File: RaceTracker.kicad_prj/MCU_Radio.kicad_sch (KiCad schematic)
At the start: 46 parts, among them J12 SWD-Programmierheader, Q1 2N7002, Q5 BSS138PS, U1 D21G18, U2 NINA-W102, Y1 32768Hz

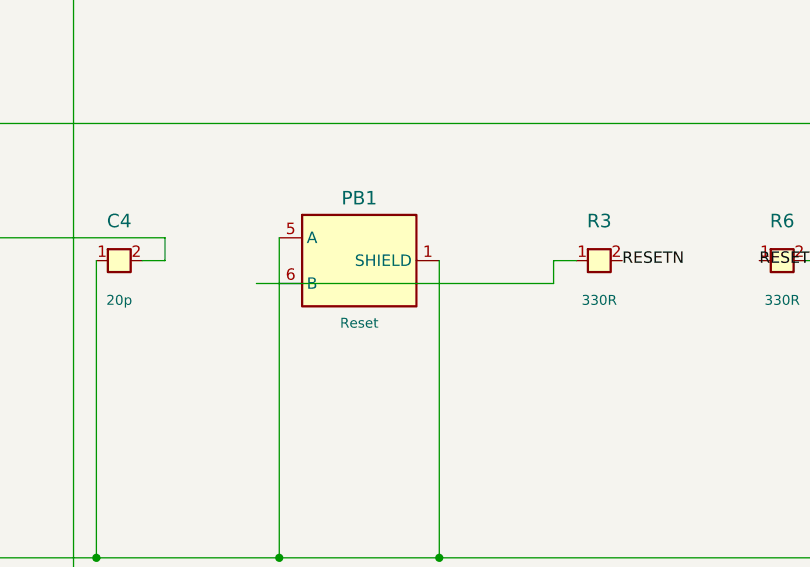
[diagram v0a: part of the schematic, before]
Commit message: ERC auf 0/0: J1.CC2/R38, J7-Draht und PB1/R3 verbunden, VBUS-Cap ergänzt
Echte KiCad-ERC (kicad-cli sch erc) fand 7 Verstöße, alle auf dasselbe
Muster zurückgeführt: ein Bauteil-Pin lag exakt auf einem Draht, aber
ohne Endpunkt-Treffer oder Junction erkannt daher KiCad ihn nicht als
verbunden. Behoben durch Draht-Trimming auf die exakte Pin-Position,
verifiziert per kicad-cli-Netzlisten-Diff (nur die betroffenen Pins
ändern sich, sonst nichts an den 128 Bauteilen):

- Power.kicad_sch: J1.CC2 <-> R38 (5,1k Pulldown) verbunden, gleicher
  Fehlertyp wie der CC1/GND-Kurzschluss aus dem letzten Commit, nur
  diesmal eine offene statt einer kurzgeschlossenen Verbindung
- Power.kicad_sch: J7.BATT+ Draht-Überstand über den Steckerkörper
  hinaus entfernt
- MCU_Radio.kicad_sch: PB1 (Reset-Taster) Pin 6 <-> R3 verbunden
- Power.kicad_sch: C34 (1uF) als VBUS-Entkopplung an J1 ergänzt, war
  direkt am USB-C-Stecker komplett unbestückt

Per Datenblatt (TI BQ24195L, u-blox ZED-F9P) als Fehlalarme der
kicad-happy-Analyse verifiziert, keine Änderung nötig: I2C_SCL/SDA
Spannungsdomäne (SCL/SDA sind Open-Drain), STAT/CE fehlender Pull-up
(STAT hat LED+R23, CE hat bewusst R25 als Pull-down), RTK_STAT/GEO_STAT
(Push-Pull-Ausgänge), CHG_VBUS ohne DC-Pfad (Analyzer modelliert keine
Transistor-Leitpfade, Q2 ist ein Standard-P-FET-Passschalter).

Co-Authored-By: Claude Sonnet 5 <noreply@anthropic.com>
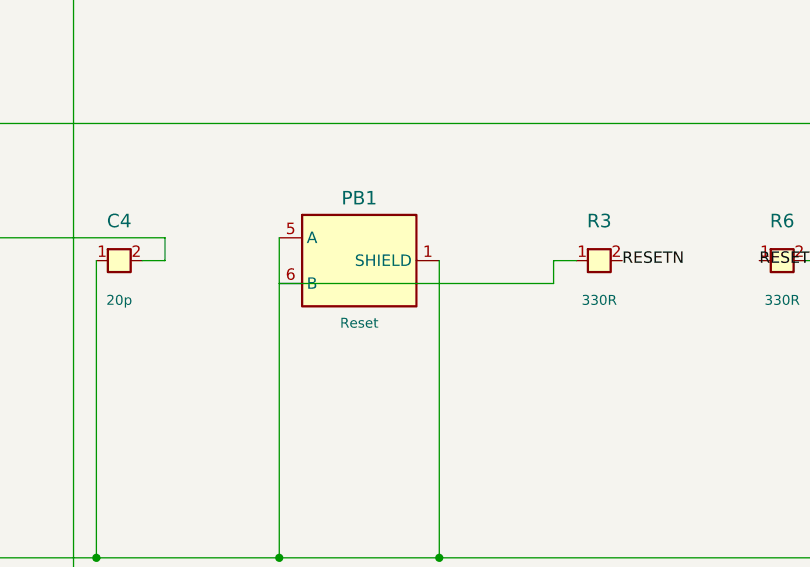
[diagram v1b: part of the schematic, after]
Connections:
- net at R3.1: now also PB1.6 (B)
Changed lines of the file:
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@@
 	(wire
 		(pts
-			(xy 78.74 156.21) (xy 111.76 156.21)
+			(xy 81.28 156.21) (xy 111.76 156.21)
 		)
 		(stroke

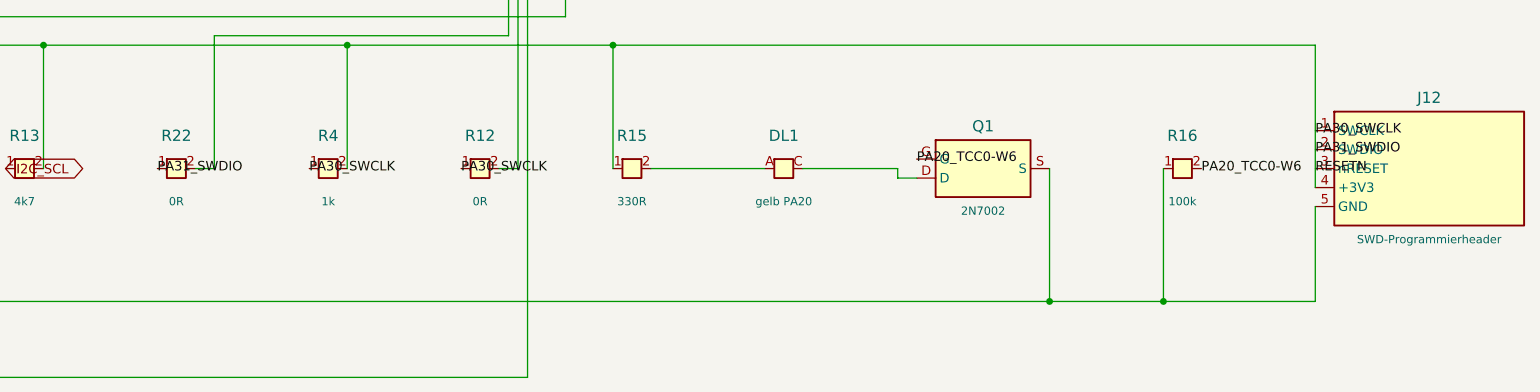
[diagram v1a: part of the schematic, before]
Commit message: Referenzabgleich gegen MKR-WiFi-1010-Eagle-Schaltplan: 2 Abweichungen behoben
Systematischer Netz-für-Netz-Vergleich zwischen der originalen Eagle-
Referenz (MKRWiFi1010V2.0.sch) und der aktuellen KiCad-Netzliste ergab
78 von 85 Netzen exakt identisch. Die restlichen 7 waren bis auf zwei
reine Pin-Namens-/Nummerierungsunterschiede zwischen Eagle- und
KiCad-Symbolen (Q5 Multi-Gate-Split, PB1-Kontaktnummerierung, J7/Q2
Pin-Namen) — keine echten Fehler.

Zwei echte Abweichungen behoben:

- MCU_Radio.kicad_sch: Serienwiderstand R2 (39R) am Reset-Pin des
  SWD-Headers ergänzt. War beim Umbau von MKR-Debug-Header (J2,
  entfallen) auf den neuen SWD-Header (J12) verlorengegangen — SWCLK
  (R4/R12) und SWDIO (R22) hatten ihre Schutzwiderstände behalten,
  nur nRESET nicht. J12.3 hängt jetzt über R2 am RESETN-Netz statt
  direkt.
- Power.kicad_sch: Label "VIN" am Netz R19.2/Q2.Gate/Q2.Anode wieder
  ergänzt (elektrisch war die Verbindung bereits korrekt, nur ohne
  Beschriftung als automatisch benanntes Netz sichtbar).

Beide Änderungen per kicad-cli-Netzlisten-Diff verifiziert (nur die
vier betroffenen Pins ändern sich), ERC weiterhin 0 Fehler/0 Warnungen.

Co-Authored-By: Claude Sonnet 5 <noreply@anthropic.com>
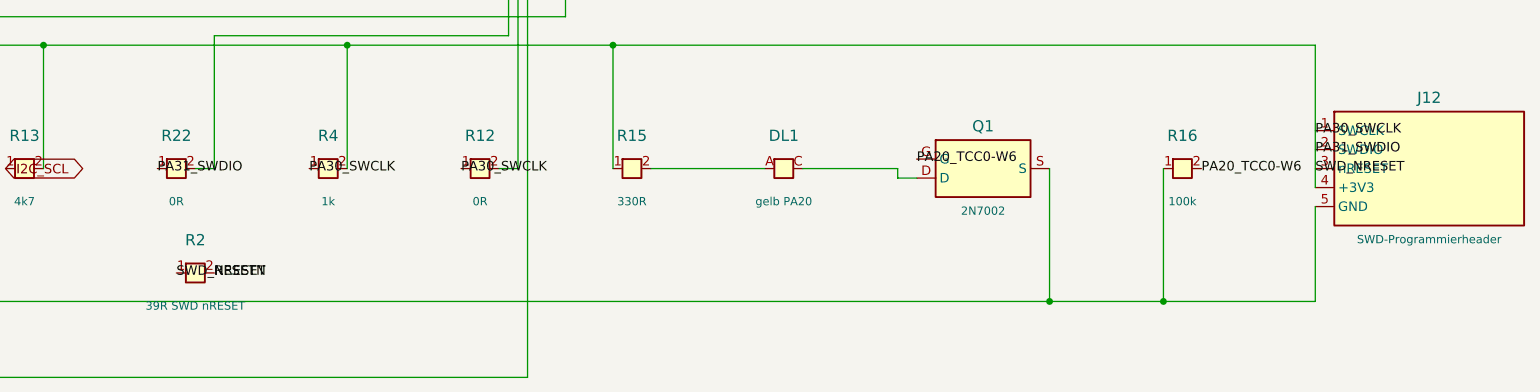
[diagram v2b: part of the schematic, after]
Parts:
- added R2: 39R SWD nRESET, symbol RaceTracker:R_GENERIC
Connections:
- net +3V3: now also R2.1; no longer C2.1, R3.2, R5.1, R6.1, U1.40 (RESETN)
- new net RESETN: C2.1, R2.2, R3.2, R5.1, R6.1, U1.40 (RESETN)
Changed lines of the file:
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@@
 		)
 	)
-	(label "RESETN"
+	(label "SWD_NRESET"
 		(at 400.05 217.17 0)
 		(effects
@@
 		)
 	)
+	(symbol
+		(lib_id "RaceTracker:R_GENERIC")
+		(at 250.19 231.14 0)
+		(unit 1)
+		(body_style 1)
+		(exclude_from_sim no)
+		(in_bom yes)
+		(on_board yes)
+		(in_pos_files yes)
+		(dnp no)
+		(property "Reference" "R2"
+			(at 250.19 226.74 0)
+			(show_name no)
+			(do_not_autoplace no)
+			(effects
+				(font
+					(size 1.5 1.5)
+				)
+			)
+		)
+		(property "Value" "39R SWD nRESET"
+			(at 250.19 235.54 0)
+			(show_name no)
+			(do_not_autoplace no)
+			(effects
+				(font
+					(size 1.1 1.1)
+				)
+			)
+		)
+		(property "Footprint" ""
+			(at 250.19 231.14 0)
+			(hide yes)
+			(show_name no)
+			(do_not_autoplace no)
+			(effects
+				(font
+					(size 1.27 1.27)
+				)
+			)
+		)
+		(property "Datasheet" ""
+			(at 250.19 231.14 0)
+			(hide yes)
+			(show_name no)
+			(do_not_autoplace no)
+			(effects
+				(font
+					(size 1.27 1.27)
+				)
+			)
+		)
+		(property "Description" ""
+			(at 250.19 231.14 0)
+			(show_name no)
+			(do_not_autoplace no)
+			(effects
+				(font
+					(size 1.27 1.27)
+				)
+			)
+		)
+		(pin "1"
+		)
+		(pin "2"
+		)
+		(instances
+			(project "RaceTracker"
+				(path "/91b37a92-c006-41eb-be41-a2390c5c45b2/2eab94b4-4968-4af9-95bb-7d350df3d3fd"
+					(reference "R2")
+					(unit 1)
+				)
+			)
+		)
+	)
+	(label "SWD_NRESET"
+		(at 247.65 231.14 0)
+		(effects
+			(font
+				(size 1.27 1.27)
+			)
+			(justify left)
+		)
+	)
+	(label "RESETN"
+		(at 252.73 231.14 0)
+		(effects
+			(font
+				(size 1.27 1.27)
+			)
+			(justify left)
+		)
+	)

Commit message: Footprints für Power+MCU_Radio: aus MKR1010-Eagle-Referenz importiert
Nutzt kicad-cli pcb import, um die reale MKR-WiFi-1010-Platine
(user-bereitgestellt, MKRWiFi1010V2.0.brd) nach KiCad zu konvertieren
und daraus bewährte, aus einem tatsächlich gefertigten Board stammende
Footprint-Geometrien zu extrahieren statt sie zu schätzen:

- 15 spezielle Footprints neu in RaceTracker.pretty/ (SOT-143B für D1,
  SOD-323FL für D2/D3, SOT-523 für Q1/Q3, SON-8 für Q2, SOT-363 für Q5,
  JST-PH für J7, PTS820-Taster, 0603-LED, RGB-5050-LED, SRP4020-Spule,
  32.768kHz-Quarz ABS07)
- 3 bestehende Custom-Footprints (QFN24, QFN48/SAMD21, NINA-W1X) durch
  die vollständigeren Eagle-Varianten ersetzt (identische Pad-Namen
  verifiziert, jetzt mit Silkscreen-Outline und Lötstoppmasken-Angaben)
- Alle Standard-Passiva (R/C 0402/0603/0805, Fuse, Ferritperle) auf
  KiCads Standardbibliothek gemappt
- J12 (SWD-Header) auf Standard-2,54mm-5-Pin-Stiftleiste gemappt

87 von 90 Bauteilen auf Power+MCU_Radio haben jetzt ein Footprint
(Rest: GPS- und Sensors_Storage-Blatt folgen). ERC weiterhin 0/0,
inklusive der Footprint-Bibliotheksprüfung (jeder Footprint-Name
gegen die echte Bibliothek verifiziert).

Co-Authored-By: Claude Sonnet 5 <noreply@anthropic.com>
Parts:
- C17, C18, C2, C21, C23, C24, C25, C26, C3, C4, C5, C6, C7: footprint (none) -> Capacitor_SMD:C_0402_1005Metric
- C27: footprint (none) -> Capacitor_SMD:C_0603_1608Metric
- DL1: footprint (none) -> RaceTracker:LED_0603_AK
- DL4: footprint (none) -> RaceTracker:RGBLED_5050
- J12: footprint (none) -> Connector_PinHeader_2.54mm:PinHeader_1x05_P2.54mm_Vertical
- L3: footprint (none) -> Inductor_SMD:L_0603_1608Metric
- PB1: footprint (none) -> RaceTracker:PTS820_NO_HOLES
- Q1: footprint (none) -> RaceTracker:SOTFL50P160X78-3
- Q5: footprint (none) -> RaceTracker:SOT363
- R10, R11, R12, R13, R14, R15, R16, R17, R18, R2, R20, R21, R22, R3, R34, R35, R36, R4, R5, R6, R7, R8, R9: footprint (none) -> Resistor_SMD:R_0402_1005Metric
- U1: footprint (none) -> RaceTracker:QFN48_SAMD21G18A
- U2: footprint (none) -> RaceTracker:NINA_W1X_MODULE
- Y1: footprint (none) -> RaceTracker:ABS07_CRYSTAL
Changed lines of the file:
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@@
 			)
 		)
-		(property "Footprint" ""
+		(property "Footprint" "RaceTracker:SOTFL50P160X78-3"
 			(at 355.6 217.17 0)
 			(hide yes)
@@
 			)
 		)
-		(property "Footprint" ""
+		(property "Footprint" "Resistor_SMD:R_0402_1005Metric"
 			(at 247.65 217.17 0)
 			(hide yes)
@@
 			)
 		)
-		(property "Footprint" ""
+		(property "Footprint" "Resistor_SMD:R_0402_1005Metric"
 			(at 250.19 231.14 0)
 			(hide yes)
@@
 			)
 		)
-		(property "Footprint" ""
+		(property "Footprint" "Capacitor_SMD:C_0402_1005Metric"
 			(at 149.86 67.31 0)
 			(hide yes)
@@
 			)
 		)
-		(property "Footprint" ""
+		(property "Footprint" "Capacitor_SMD:C_0402_1005Metric"
 			(at 88.9 67.31 0)
 			(hide yes)
@@
 			)
 		)
-		(property "Footprint" ""
+		(property "Footprint" "Resistor_SMD:R_0402_1005Metric"
 			(at 337.82 153.67 0)
 			(hide yes)
@@
 			)
 		)
-		(property "Footprint" ""
+		(property "Footprint" "Resistor_SMD:R_0402_1005Metric"
 			(at 157.48 153.67 0)
 			(hide yes)
@@
 			)
 		)
-		(property "Footprint" ""
+		(property "Footprint" "Capacitor_SMD:C_0402_1005Metric"
 			(at 292.1 67.31 0)
 			(hide yes)
@@
 			)
 		)
-		(property "Footprint" ""
+		(property "Footprint" "Resistor_SMD:R_0402_1005Metric"
 			(at 227.33 217.17 0)
 			(hide yes)
@@
 			)
 		)
-		(property "Footprint" ""
+		(property "Footprint" "RaceTracker:NINA_W1X_MODULE"
 			(at 251.46 153.67 0)
 			(hide yes)
@@
 			)
 		)
-		(property "Footprint" ""
+		(property "Footprint" "Resistor_SMD:R_0402_1005Metric"
 			(at 137.16 153.67 0)
 			(hide yes)
@@
 			)
 		)
-		(property "Footprint" ""
+		(property "Footprint" "Capacitor_SMD:C_0402_1005Metric"
 			(at 210.82 67.31 0)
 			(hide yes)
@@
 			)
 		)
-		(property "Footprint" ""
+		(property "Footprint" "Capacitor_SMD:C_0402_1005Metric"
 			(at 271.78 67.31 0)
 			(hide yes)
@@
 			)
 		)
-		(property "Footprint" ""
+		(property "Footprint" "Resistor_SMD:R_0402_1005Metric"
 			(at 332.74 67.31 0)
 			(hide yes)
@@
 			)
 		)
-		(property "Footprint" ""
+		(property "Footprint" "RaceTracker:SOT363"
 			(at 69.85 217.17 0)
 			(hide yes)
@@
 			)
 		)
-		(property "Footprint" ""
+		(property "Footprint" "Capacitor_SMD:C_0402_1005Metric"
 			(at 170.18 67.31 0)
 			(hide yes)
@@
 			)
 		)
-		(property "Footprint" ""
+		(property "Footprint" "Resistor_SMD:R_0402_1005Metric"
 			(at 116.84 153.67 0)
 			(hide yes)
@@
 			)
 		)
-		(property "Footprint" ""
+		(property "Footprint" "Capacitor_SMD:C_0603_1608Metric"
 			(at 231.14 67.31 0)
 			(hide yes)
@@
 			)
 		)
-		(property "Footprint" ""
+		(property "Footprint" "Resistor_SMD:R_0402_1005Metric"
 			(at 308.61 217.17 0)
 			(hide yes)
@@
 			)
 		)
-		(property "Footprint" ""
+		(property "Footprint" "RaceTracker:SOT363"
 			(at 99.06 217.17 0)
 			(hide yes)
@@
 			)
 		)
-		(property "Footprint" ""
+		(property "Footprint" "Resistor_SMD:R_0402_1005Metric"
 			(at 43.18 217.17 0)
 			(hide yes)
@@
 			)
 		)
-		(property "Footprint" ""
+		(property "Footprint" "Resistor_SMD:R_0402_1005Metric"
 			(at 267.97 217.17 0)
 			(hide yes)
@@
 			)
 		)
-		(property "Footprint" ""
+		(property "Footprint" "Resistor_SMD:R_0402_1005Metric"
 			(at 166.37 217.17 0)
 			(hide yes)
@@
 			)
 		)
-		(property "Footprint" ""
+		(property "Footprint" "Resistor_SMD:R_0402_1005Metric"
 			(at 186.69 217.17 0)
 			(hide yes)
@@
 			)
 		)
-		(property "Footprint" ""
+		(property "Footprint" "RaceTracker:PTS820_NO_HOLES"
 			(at 90.17 153.67 0)
 			(hide yes)
@@
 			)
 		)
-		(property "Footprint" ""
+		(property "Footprint" "Resistor_SMD:R_0402_1005Metric"
 			(at 22.86 217.17 0)
 			(hide yes)
@@
 			)
 		)
-		(property "Footprint" ""
+		(property "Footprint" "Resistor_SMD:R_0402_1005Metric"
 			(at 378.46 153.67 0)
 			(hide yes)
@@
 			)
 		)
-		(property "Footprint" ""
+		(property "Footprint" "Resistor_SMD:R_0402_1005Metric"
 			(at 125.73 217.17 0)
 			(hide yes)
@@
 			)
 		)
-		(property "Footprint" ""
+		(property "Footprint" "Resistor_SMD:R_0402_1005Metric"
 			(at 207.01 217.17 0)
 			(hide yes)
@@
 			)
 		)
-		(property "Footprint" ""
+		(property "Footprint" "Resistor_SMD:R_0402_1005Metric"
 			(at 358.14 153.67 0)
 			(hide yes)
@@
 			)
 		)
-		(property "Footprint" ""
+		(property "Footprint" "RaceTracker:LED_0603_AK"
 			(at 328.93 217.17 0)
 			(hide yes)
@@
 			)
 		)
-		(property "Footprint" ""
+		(property "Footprint" "Connector_PinHeader_2.54mm:PinHeader_1x05_P2.54mm_Vertical"
 			(at 415.29 217.17 0)
 			(hide yes)
@@
 			)
 		)
-		(property "Footprint" ""
+		(property "Footprint" "Capacitor_SMD:C_0402_1005Metric"
 			(at 63.5 153.67 0)
 			(hide yes)
@@
 			)
 		)
-		(property "Footprint" ""
+		(property "Footprint" "Resistor_SMD:R_0402_1005Metric"
 			(at 198.12 153.67 0)
 			(hide yes)
@@
 			)
 		)
-		(property "Footprint" ""
+		(property "Footprint" "Capacitor_SMD:C_0402_1005Metric"
 			(at 43.18 153.67 0)
 			(hide yes)
@@
 			)
 		)
-		(property "Footprint" ""
+		(property "Footprint" "Resistor_SMD:R_0402_1005Metric"
 			(at 312.42 67.31 0)
 			(hide yes)
@@
 			)
 		)
-		(property "Footprint" ""
+		(property "Footprint" "Resistor_SMD:R_0402_1005Metric"
 			(at 288.29 217.17 0)
 			(hide yes)
@@
 			)
 		)
-		(property "Footprint" ""
+		(property "Footprint" "Resistor_SMD:R_0402_1005Metric"
 			(at 146.05 217.17 0)
 			(hide yes)
@@
 			)
 		)
-		(property "Footprint" ""
+		(property "Footprint" "RaceTracker:ABS07_CRYSTAL"
 			(at 22.86 153.67 0)
 			(hide yes)
@@
 			)
 		)
-		(property "Footprint" ""
+		(property "Footprint" "Capacitor_SMD:C_0402_1005Metric"
 			(at 129.54 67.31 0)
 			(hide yes)
@@
 			)
 		)
-		(property "Footprint" ""
+		(property "Footprint" "Resistor_SMD:R_0402_1005Metric"
 			(at 382.27 217.17 0)
 			(hide yes)
@@
 			)
 		)
-		(property "Footprint" ""
+		(property "Footprint" "Capacitor_SMD:C_0402_1005Metric"
 			(at 68.58 67.31 0)
 			(hide yes)
@@
 			)
 		)
-		(property "Footprint" ""
+		(property "Footprint" "Inductor_SMD:L_0603_1608Metric"
 			(at 190.5 67.31 0)
 			(hide yes)
@@
 			)
 		)
-		(property "Footprint" ""
+		(property "Footprint" "Capacitor_SMD:C_0402_1005Metric"
 			(at 251.46 67.31 0)
 			(hide yes)
@@
 			)
 		)
-		(property "Footprint" ""
+		(property "Footprint" "RaceTracker:RGBLED_5050"
 			(at 311.15 153.67 0)
 			(hide yes)
@@
 			)
 		)
-		(property "Footprint" ""
+		(property "Footprint" "RaceTracker:QFN48_SAMD21G18A"
 			(at 35.56 67.31 0)
 			(hide yes)
@@
 			)
 		)
-		(property "Footprint" ""
+		(property "Footprint" "Capacitor_SMD:C_0402_1005Metric"
 			(at 109.22 67.31 0)
 			(hide yes)
@@
 			)
 		)
-		(property "Footprint" ""
+		(property "Footprint" "Capacitor_SMD:C_0402_1005Metric"
 			(at 177.8 153.67 0)
 			(hide yes)
